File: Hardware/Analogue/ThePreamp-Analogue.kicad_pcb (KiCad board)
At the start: 2 copper layers, 60 x 95.8 mm, 34 parts, among them J1 B1 Relays, J10 I2C (FUTURE USE), J11 ROTARY ENC & SWITCH 1, J12 ROTARY ENC & SWITCH 2, J13 IR RECV, J14 12V, J15 8V, J2 PWR AMP L 12V TRIGGER, J3 PWR AMP L SWITCH, J4 PWR AMP R 12V TRIGGER, J5 PWR AMP R SWITCH, J6 PWR AMP TEMP NTC L, J7 PWR AMP TEMP NTC R, J8 MUSES 72320 (SPI), J9 I2C DISPLAY (OLED/LCD), U1 AGQ20T03, U2 AGQ20T03, U3 ULN2803ADWR, U4 MCP23008-E_SO, U5 24C02C_SN, U6 ESP32-DEVKIT-V1

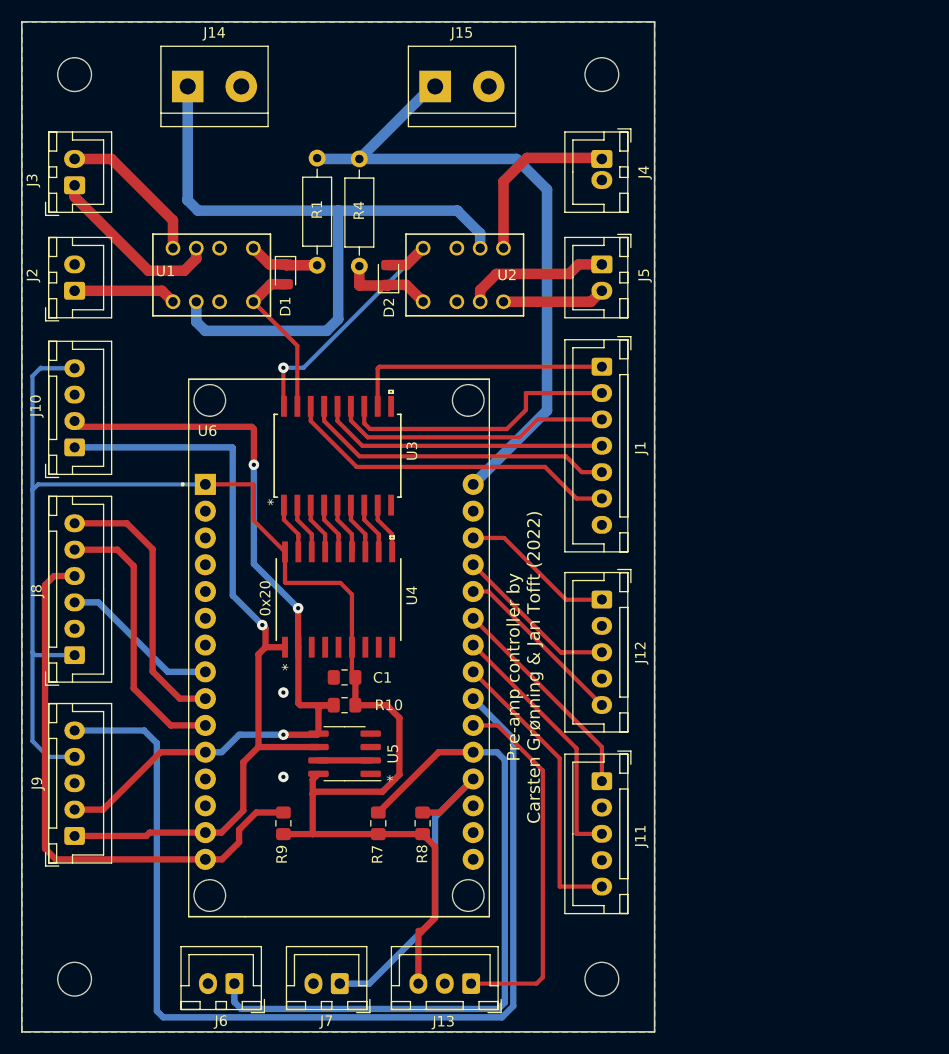
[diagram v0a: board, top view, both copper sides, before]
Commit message: added footprint to rca connector
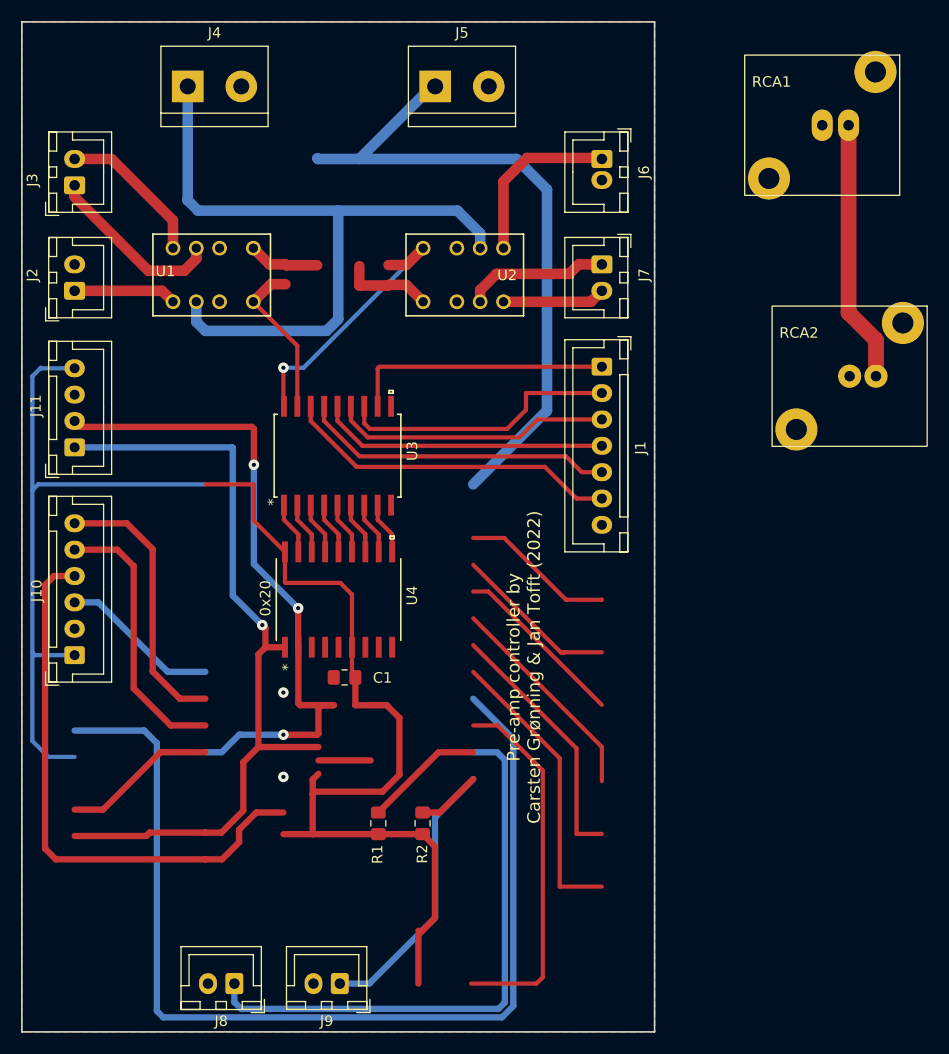
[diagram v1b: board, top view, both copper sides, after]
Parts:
- removed D1, D2: CD4148W, Diode_SMD:D_0805_2012Metric
- removed the J11 at (175.0, 122.0)
- removed J12: ROTARY ENC & SWITCH 2, Connector_JST:JST_XH_B5B-XH-A_1x05_P2.50mm_Vertical
- removed J13: IR RECV, Connector_JST:JST_XH_B3B-XH-A_1x03_P2.50mm_Vertical
- removed the J9 at (125.0, 127.2)
- removed the R1 at (148.0, 62.9)
- removed R10, R9: 4K7, Resistor_SMD:R_0805_2012Metric_Pad1.15x1.40mm_HandSolder
- removed R4: R, Resistor_THT:R_Axial_DIN0207_L6.3mm_D2.5mm_P10.16mm_Horizontal
- removed REF** (x4): MountingHole_3.2mm_M3_ISO7380, MountingHole:MountingHole_3.2mm_M3_ISO7380
- removed U5: 24C02C_SN, Package_SO:SOIC-8-1EP_3.9x4.9mm_P1.27mm_EP2.41x3.3mm
- removed U6: ESP32-DEVKIT-V1, ESP32FP:MODULE_ESP32_DEVKIT_V1
- added RCA1: RCA_Connector_ALI, Connector_Audio:RCA Connector ALI, F.Cu at (188.5, 53.1)
- added RCA2: RCA_Connector_ALI, Connector_Audio:RCA Connector ALI, F.Cu at (191.1, 77.0)
- renumbered J8 to J10, J10 to J11, J14 to J4, J15 to J5, J4 to J6, J5 to J7, J6 to J8, J7 to J9, R7 to R1, R8 to R2
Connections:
- U1 pad 1: Net-(D1-Pad1) -> +12V
- U2 pad 1: Net-(D2-Pad1) -> +12V
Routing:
- net (no net): track 0.00 -> 253.5 mm
- net CONTRAST(LCD): track 98.9 -> 0.00 mm
- net IR OUT: track 35.0 -> 0.00 mm
- net CW_1: track 27.8 -> 0.00 mm
- net GND: track 4.95 -> 29.8 mm
- net CCW_1: track 24.4 -> 0.00 mm
- net SW_1: track 20.5 -> 0.00 mm
- net CW_2: track 16.7 -> 0.00 mm
- net CCW_2: track 15.7 -> 0.00 mm
- net +12V: track 67.7 -> 83.0 mm
- net SW_2: track 14.6 -> 0.00 mm
- net Net-(D2-Pad1): track 8.58 -> 0.00 mm
- net Net-(D1-Pad1): track 6.72 -> 0.00 mm

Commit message: Added input section
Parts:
- removed the J1 at (175.0, 82.7)
- added K1: EA2-12NJ, EA2-12NJ:DIPS762W60P254L1420H630Q10N, F.Cu at (65.2, 32.8)
- added K2: EA2-12NJ, EA2-12NJ:DIPS762W60P254L1420H630Q10N, F.Cu at (54.5, 32.8)
- added K3: EA2-12NJ, EA2-12NJ:DIPS762W60P254L1420H630Q10N, F.Cu at (43.7, 32.8)
- renumbered J4 to J1, J11 to J10, J8 to J2, J9 to J3, J2 to J4, J3 to J5, J5 to J6, J6 to J7, J7 to J8, J10 to J9, U3 to U2, U2 to U3
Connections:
- J1 pad 1: +12V -> unconnected-(J1-Pad1)
- J1 pad 2: GND -> unconnected-(J1-Pad2)
- RCA2 pad 2: GND -> unconnected-(RCA2-Pad2)
- U1 pad 8: Net-(U1-Pad8) -> unconnected-(U1-Pad8)
- U2 pad 11: Net-(J1-Pad1) -> RELAY1
- U2 pad 12: Net-(J1-Pad2) -> RELAY2
- U2 pad 13: Net-(J1-Pad3) -> RELAY3
- U2 pad 14: Net-(J1-Pad4) -> RELAY4
- U2 pad 15: Net-(J1-Pad5) -> RELAY5
- U2 pad 16: Net-(J1-Pad6) -> RELAY6
- U2 pad 17: Net-(U1-Pad8) -> RELAY7
- U2 pad 18: Net-(U2-Pad8) (its old number) -> RELAY8
- U3 pad 8: Net-(U2-Pad8) (its old number) -> unconnected-(U3-Pad8)
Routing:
- net RELAY6: track 0.00 -> 32.0 mm
- net Net-(J1-Pad6): track 32.0 -> 0.00 mm
- net RELAY5: track 0.00 -> 29.7 mm
- net Net-(J1-Pad5): track 29.7 -> 0.00 mm
- net RELAY4: track 0.00 -> 27.4 mm
- net Net-(J1-Pad4): track 27.4 -> 0.00 mm
- net RELAY2: track 0.00 -> 26.7 mm
- net Net-(J1-Pad2): track 26.7 -> 0.00 mm
- net RELAY3: track 0.00 -> 26.5 mm
- net Net-(J1-Pad3): track 26.5 -> 0.00 mm
- net RELAY8: track 0.00 -> 25.6 mm, vias 0 -> 1
- net Net-(U2-Pad8) (its old number): track 25.6 -> 0.00 mm, vias 1 -> 0
- net RELAY1: track 0.00 -> 24.9 mm
- net Net-(J1-Pad1): track 24.9 -> 0.00 mm
- net unconnected-(RCA2-Pad2): track 0.00 -> 24.9 mm
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
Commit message: seperate kicad project for buffer
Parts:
- removed C1: 0.1uF, Capacitor_SMD:C_0805_2012Metric_Pad1.15x1.40mm_HandSolder
- removed J10: I2C (FUTURE USE), Connector_JST:JST_XH_B4B-XH-A_1x04_P2.50mm_Vertical
- removed K1, K2, K3: EA2-12NJ, EA2-12NJ:DIPS762W60P254L1420H630Q10N
- removed R1, R2: 10K, Resistor_SMD:R_0805_2012Metric_Pad1.15x1.40mm_HandSolder
- removed U1, U3: AGQ20T03, AGQ20T03_footprint:AGQ20012
- removed U2: ULN2803ADWR, ULN2803:ULN2803ADWR
- removed U4: MCP23008-E_SO, MCP23008:MCP23008-E&slash_SO
- added C12: 100 uf/25V, Capacitor_THT:CP_Radial_D8.0mm_P3.50mm, F.Cu at (-24.0, 19.4)
- added C13: 100 uf/25V, Capacitor_THT:CP_Radial_D8.0mm_P3.50mm, F.Cu at (-16.1, 7.75)
- added C14: 100 uf/25V, Capacitor_THT:CP_Radial_D8.0mm_P3.50mm, F.Cu at (3.31, -16.9)
- added C15: 100 uf/25V, Capacitor_THT:CP_Radial_D8.0mm_P3.50mm, F.Cu at (24.6, -25.9)
- added C2: 100 uf/25V, Capacitor_THT:CP_Radial_D8.0mm_P3.50mm, F.Cu at (-6.40, -1.80)
- added C3: 100 uf/25V, Capacitor_THT:CP_Radial_D8.0mm_P3.50mm, F.Cu at (14.9, -25.9)
- added C4: 10 uf/50V, Capacitor_THT:CP_Radial_D8.0mm_P3.50mm, F.Cu at (-33.7, 19.4)
- added C5: 100 uf/25V, Capacitor_THT:CP_Radial_D8.0mm_P3.50mm, F.Cu at (13.1, -16.4)
- added C7: 100 uf/25V, Capacitor_THT:CP_Radial_D8.0mm_P3.50mm, F.Cu at (-16.1, -1.80)
- added RCA10: RCA_Connector_ALI, Connector_Audio:RCA Connector ALI, F.Cu at (-50.6, -14.7)
- added RCA3: RCA_Connector_ALI, Connector_Audio:RCA Connector ALI, F.Cu at (-66.6, -6.92)
- added RCA4: RCA_Connector_ALI, Connector_Audio:RCA Connector ALI, F.Cu at (-31.2, -29.8)
- added RCA5: RCA_Connector_ALI, Connector_Audio:RCA Connector ALI, F.Cu at (-66.6, -22.0)
- added RCA6: RCA_Connector_ALI, Connector_Audio:RCA Connector ALI, F.Cu at (-34.6, 0.38)
- added RCA7: RCA_Connector_ALI, Connector_Audio:RCA Connector ALI, F.Cu at (-15.2, -29.8)
- added RCA8: RCA_Connector_ALI, Connector_Audio:RCA Connector ALI, F.Cu at (-66.6, 8.18)
- added RCA9: RCA_Connector_ALI, Connector_Audio:RCA Connector ALI, F.Cu at (-47.2, -29.8)
- J1: value 12V -> PWR AMP TEMP NTC L; footprint TerminalBlock:TerminalBlock_bornier-2_P5.08mm -> Connector_JST:JST_XH_B2B-XH-A_1x02_P2.50mm_Vertical
- J2: value PWR AMP TEMP NTC L -> PWR AMP TEMP NTC R
- J3: value PWR AMP TEMP NTC R -> 8V; footprint Connector_JST:JST_XH_B2B-XH-A_1x02_P2.50mm_Vertical -> TerminalBlock:TerminalBlock_bornier-2_P5.08mm
- J4: value PWR AMP L 12V TRIGGER -> 12V; footprint Connector_JST:JST_XH_B2B-XH-A_1x02_P2.50mm_Vertical -> TerminalBlock:TerminalBlock_bornier-2_P5.08mm
- J5: value PWR AMP L SWITCH -> I2C; footprint Connector_JST:JST_XH_B2B-XH-A_1x02_P2.50mm_Vertical -> Connector_JST:JST_XH_B4B-XH-A_1x04_P2.50mm_Vertical
- J6: value 8V -> SPI; footprint TerminalBlock:TerminalBlock_bornier-2_P5.08mm -> Connector_JST:JST_XH_B6B-XH-A_1x06_P2.50mm_Vertical
- J7: value PWR AMP R 12V TRIGGER -> Conn_01x03_Female; footprint Connector_JST:JST_XH_B2B-XH-A_1x02_P2.50mm_Vertical -> Connector_PinHeader_2.54mm:PinHeader_1x03_P2.54mm_Vertical
- J8: value PWR AMP R SWITCH -> Conn_01x03_Female; footprint Connector_JST:JST_XH_B2B-XH-A_1x02_P2.50mm_Vertical -> Connector_PinHeader_2.54mm:PinHeader_1x03_P2.54mm_Vertical
- J9: value MUSES 72320 (SPI) -> Conn_01x03_Female; footprint Connector_JST:JST_XH_B6B-XH-A_1x06_P2.50mm_Vertical -> Connector_PinHeader_2.54mm:PinHeader_1x03_P2.54mm_Vertical
- moved RCA1 244.9 mm to (-50.6, 0.38)
- moved RCA2 243.7 mm to (-34.6, -14.7)
- moved J6 238.2 mm to (-63.9, -27.4)
- moved J3 222.7 mm to (3.33, -26.2), turned to 0 degrees
- moved J2 202.8 mm to (3.60, -8.75), turned to 0 degrees
- moved J8 191.3 mm to (-9.90, 24.0), turned to 0 degrees
- moved J7 179.9 mm to (-0.60, 24.0), turned to 0 degrees
- moved J5 179.3 mm to (-47.9, 17.9), turned to 0 degrees
- moved J4 165.6 mm to (-16.1, -11.1), turned to 0 degrees
- moved J9 156.1 mm to (-5.25, 24.0), turned to 0 degrees
- moved J1 150.3 mm to (-6.14, 6.35)
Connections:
- J1 pad 1: unconnected-(J1-Pad1) -> NTC_L
- J1 pad 2: unconnected-(J1-Pad2) -> GND
- J2 pad 1: NTC_L -> NTC_R
- J3 pad 1: NTC_R -> +8V
- J4 pad 1: Net-(J4-Pad1) -> unconnected-(J4-Pad1)
- J4 pad 2: GND -> unconnected-(J4-Pad2)
- J5 pad 1: Net-(J5-Pad1) -> I2C:SCL
- J5 pad 2: Net-(J5-Pad2) -> I2C:SDA
- J6 pad 1: +8V -> +3V3
- J7 pad 1: Net-(J7-Pad1) -> +15V
- J8 pad 1: Net-(J8-Pad1) -> OUTL
- J8 pad 2: Net-(J8-Pad2) -> L-
- J9 pad 1: +3V3 -> OUTR
- J9 pad 2: GND -> R-
- J9 pad 3: SPI:SS -> R+
- RCA1 pad 1: unconnected-(RCA1-Pad1) -> Net-(K1-Pad3)
- RCA1 pad 2: GND -> GNDA
- RCA2 pad 1: unconnected-(RCA2-Pad1) -> Net-(K2-Pad3)
- RCA2 pad 2: unconnected-(RCA2-Pad2) -> GNDA
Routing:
- net (no net): track 253.5 -> 0.00 mm
- net +3V3: track 150.7 -> 0.00 mm
- net +12V: track 83.0 -> 0.00 mm
- net I2C:SDA: track 78.6 -> 0.00 mm, vias 3 -> 0
- net I2C:SCL: track 76.1 -> 0.00 mm, vias 1 -> 0
- net NTC_L: track 65.6 -> 0.00 mm
- net +8V: track 63.9 -> 0.00 mm
- net SPI:MOSI: track 53.7 -> 0.00 mm
- net NTC_R: track 32.4 -> 0.00 mm
- net RELAY6: track 32.0 -> 0.00 mm
- net RELAY5: track 29.7 -> 0.00 mm
- net RELAY4: track 27.4 -> 0.00 mm
- net RELAY2: track 26.7 -> 0.00 mm
- net RELAY3: track 26.5 -> 0.00 mm
- net SPI:MISO: track 26.1 -> 0.00 mm
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- removed copper zone on B.Cu, net GND
- removed copper zone on F.Cu, net GND
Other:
- board outline removed
- board text removed: "0x20"
- board text removed: "Pre-amp controller by Carsten Grønning & Jan Tofft (2022)"

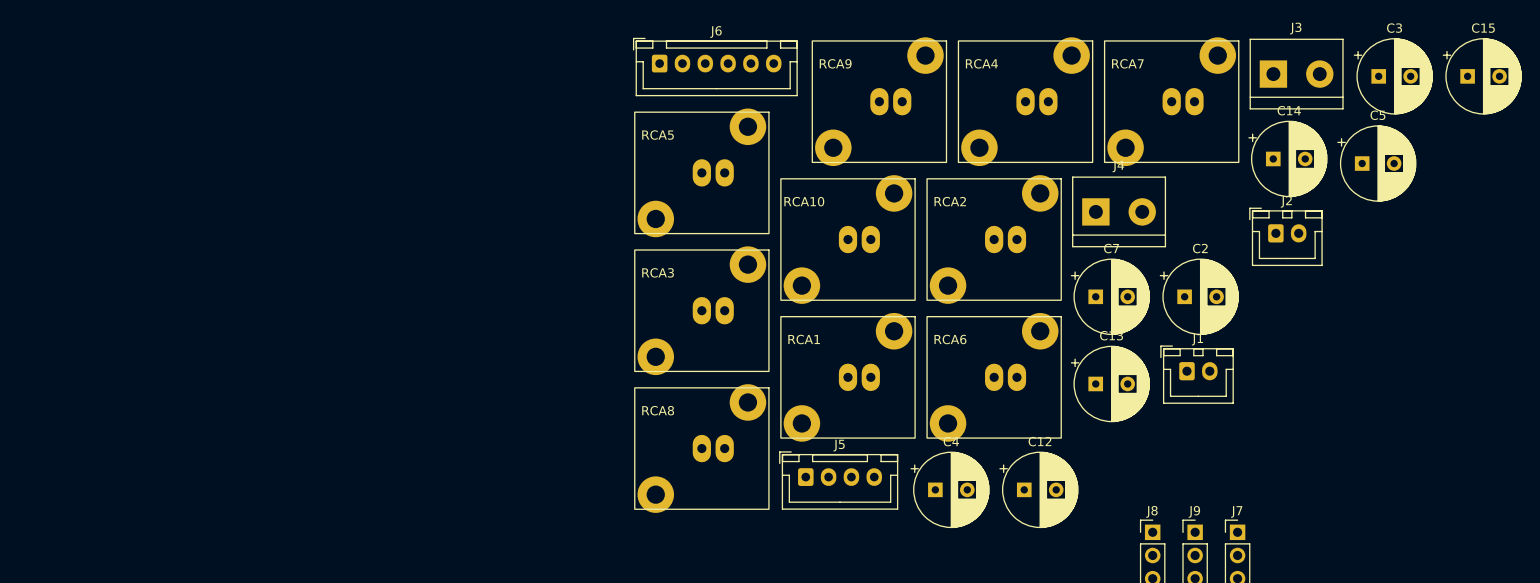
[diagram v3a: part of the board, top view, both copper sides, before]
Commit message: update analogue schematic
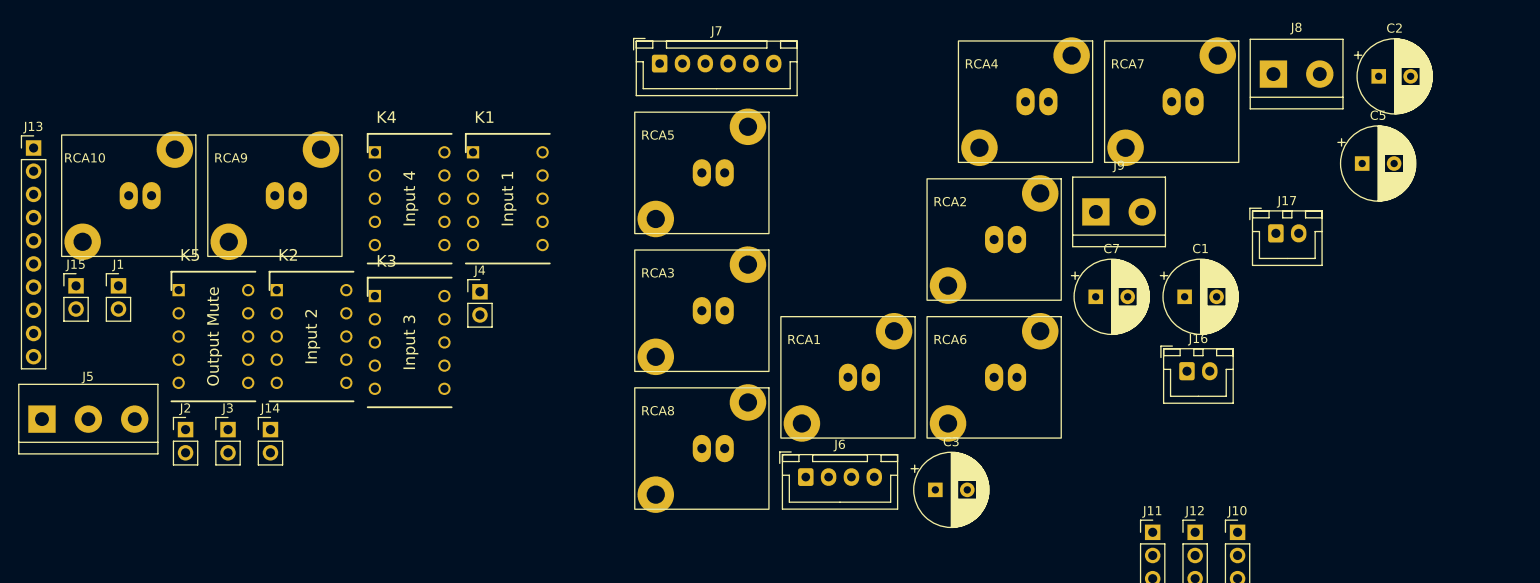
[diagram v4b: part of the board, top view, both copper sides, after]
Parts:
- removed C12, C13, C14, C15: 100 uf/25V, Capacitor_THT:CP_Radial_D8.0mm_P3.50mm
- added J1: Audio In Left, Connector_PinHeader_2.54mm:PinHeader_1x02_P2.54mm_Vertical, F.Cu at (-123.2, -3.00)
- added J13: ADS1115, Connector_PinHeader_2.54mm:PinHeader_1x10_P2.54mm_Vertical, F.Cu at (-132.5, -18.1)
- added J14: Buffer Out Right, Connector_PinHeader_2.54mm:PinHeader_1x02_P2.54mm_Vertical, F.Cu at (-106.5, 12.8)
- added J15: Buffer Out Left, Connector_PinHeader_2.54mm:PinHeader_1x02_P2.54mm_Vertical, F.Cu at (-127.8, -3.00)
- added J2: Audio In Right, Connector_PinHeader_2.54mm:PinHeader_1x02_P2.54mm_Vertical, F.Cu at (-115.8, 12.8)
- added J3: Audio In Right, Connector_PinHeader_2.54mm:PinHeader_1x02_P2.54mm_Vertical, F.Cu at (-111.2, 12.8)
- added J4: Audio In Left, Connector_PinHeader_2.54mm:PinHeader_1x02_P2.54mm_Vertical, F.Cu at (-83.6, -2.35)
- added J5: Audio Power, TerminalBlock:TerminalBlock_bornier-3_P5.08mm, F.Cu at (-131.6, 11.6)
- added K1: Input 1, EA2-12NJ:DIPS762W60P254L1420H630Q10N, F.Cu at (-84.4, -17.6)
- added K2: Input 2, EA2-12NJ:DIPS762W60P254L1420H630Q10N, F.Cu at (-105.9, -2.53)
- added K3: Input 3, EA2-12NJ:DIPS762W60P254L1420H630Q10N, F.Cu at (-95.1, -1.88)
- added K4: Input 4, EA2-12NJ:DIPS762W60P254L1420H630Q10N, F.Cu at (-95.1, -17.6)
- added K5: Output Mute, EA2-12NJ:DIPS762W60P254L1420H630Q10N, F.Cu at (-116.6, -2.53)
- J10: renamed from J7; value Conn_01x03_Female -> Buffer Power
- J11: renamed from J8; value Conn_01x03_Female -> Buffer In Left
- J12: renamed from J9; value Conn_01x03_Female -> Buffer In Right
- J16: renamed from J1; value PWR AMP TEMP NTC L -> Replace
- J17: renamed from J2; value PWR AMP TEMP NTC R -> Replace
- J8: renamed from J3; value 8V -> Digital Power
- J9: renamed from J4; value 12V -> Relay Power
- moved RCA10 78.9 mm to (-129.4, -19.5)
- moved RCA9 67.0 mm to (-113.4, -19.5)
- renumbered C2 to C1, C3 to C2, C4 to C3, J5 to J6, J6 to J7
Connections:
- J16 pad 1: NTC_L -> A0
- J17 pad 1: NTC_R -> A1
- J8 pad 1: +8V -> +3V3
- J9 pad 1: unconnected-(J4-Pad1) -> +12V
- J9 pad 2: unconnected-(J4-Pad2) -> GND

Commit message: rca pcb layout v.0.8
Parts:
- moved RCA10 395.0 mm to (248.9, 94.1)
- moved RCA9 389.7 mm to (248.9, 124.1)
- moved RCA4 214.6 mm to (123.8, 118.6)
- moved RCA8 211.6 mm to (123.8, 100.4)
- moved RCA3 207.3 mm to (98.3, 118.6)
- moved C1 205.6 mm to (193.2, 47.7)
- moved C2 205.6 mm to (214.5, 23.6)
- moved C3 205.6 mm to (165.9, 68.9)
- moved C5 205.6 mm to (212.6, 33.1)
- moved C7 205.6 mm to (183.5, 47.7)
- moved J1 205.6 mm to (76.4, 46.5)
- moved J10 205.6 mm to (199.0, 73.5)
- moved J11 205.6 mm to (189.7, 73.5)
- moved J12 205.6 mm to (194.3, 73.5)
- moved J13 205.6 mm to (67.1, 31.4)
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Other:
- board outline added: 240 x 65 mm
